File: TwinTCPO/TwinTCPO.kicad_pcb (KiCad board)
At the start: 2 copper layers, 83.8 x 45.1 mm, 44 parts, among them J1 Power, J2 Key, J3 Spk, J4 Phone, Q1 2N4401, Q2 2N7000, Q3 2N4401, Q4 2N4401, Q5 2N4403, U1 LM386

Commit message: Sync schematic and PCB
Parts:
- R6: value 10K -> 18K
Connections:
- J2 pad 3: Net-(J2-Pad3) -> unconnected-(J2-Pad3)
- J4 pad 10: Net-(J4-Pad10) -> unconnected-(J4-Pad10)
- RV3 pad 1: Net-(RV3-Pad1) -> unconnected-(RV3-Pad1)

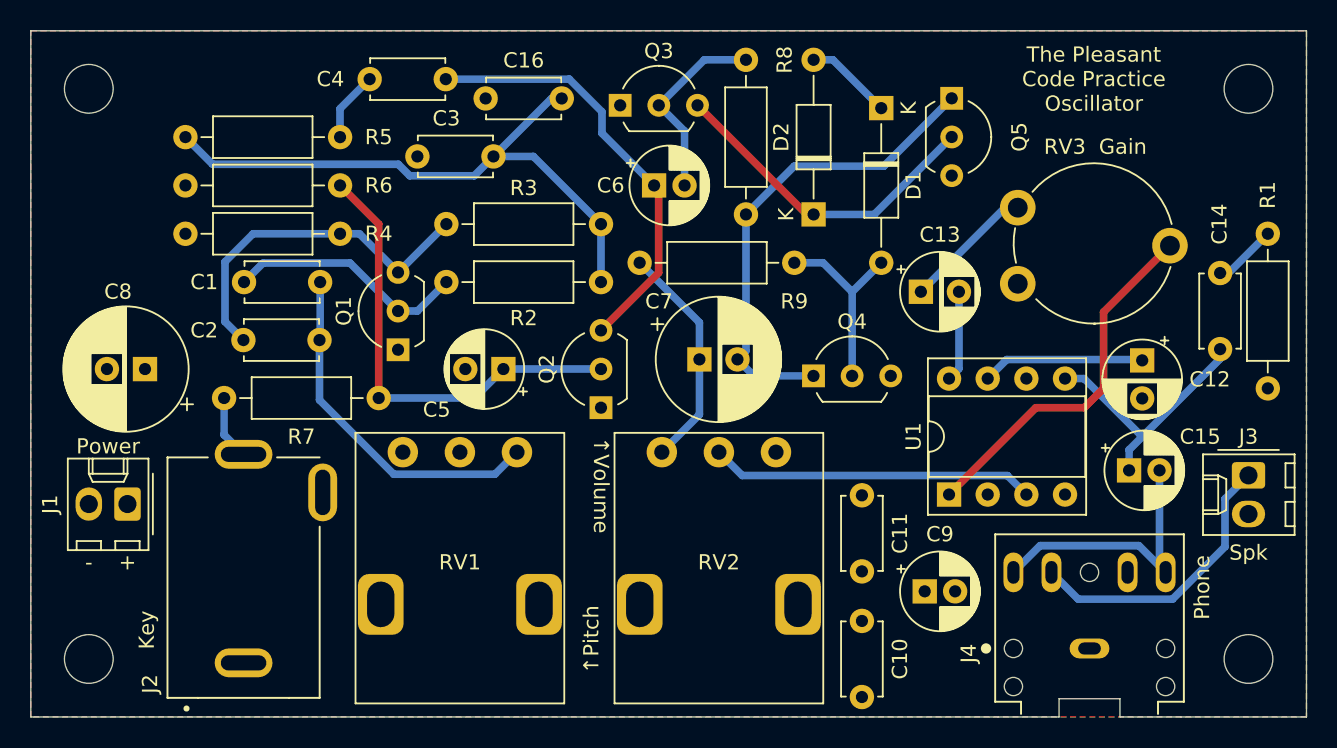
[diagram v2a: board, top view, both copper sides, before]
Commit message: Start at version 2
* Remove headphone jack
* Change R2/R3 for lower frequency
* Add 2.2K resistor in series with RV1
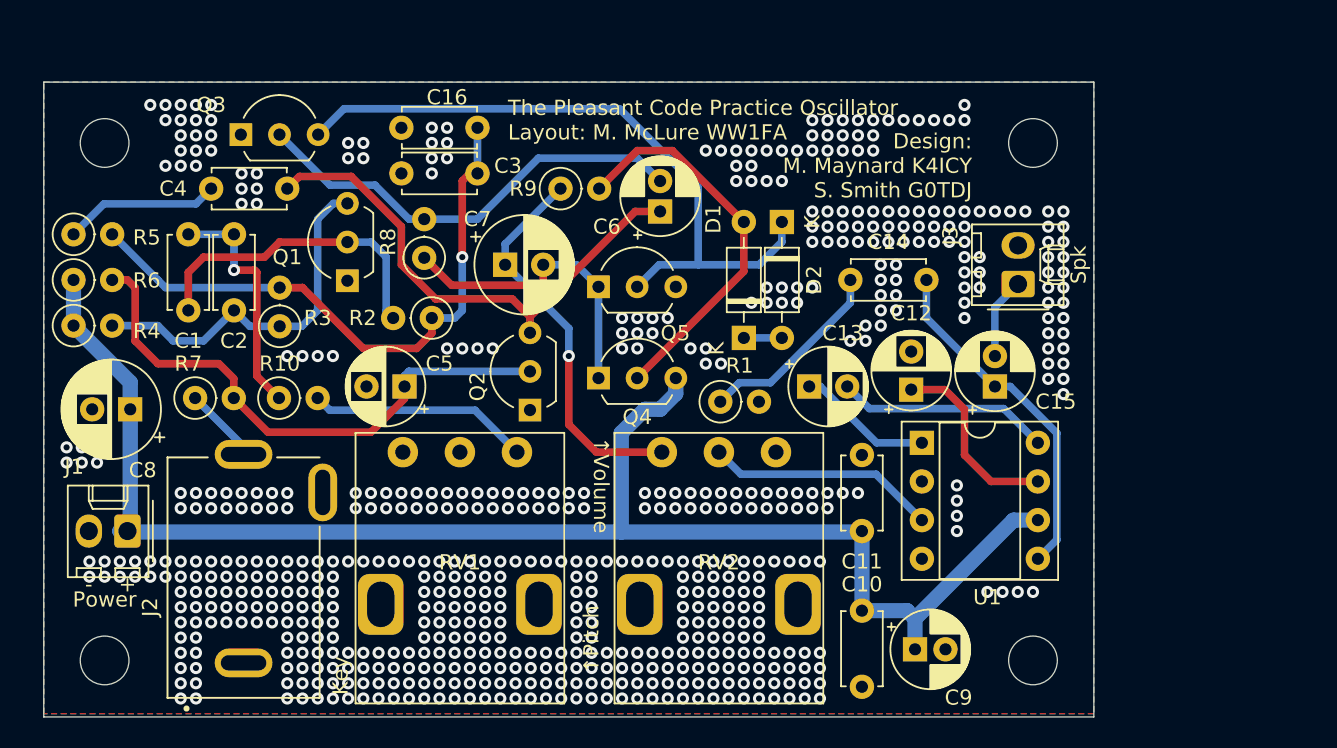
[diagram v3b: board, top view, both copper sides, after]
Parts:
- removed J4: Phone, MyLibrary:CUI_SJ1-3525N
- removed RV3: 10K, Potentiometer_THT:Potentiometer_Piher_PT-10-V10_Vertical
- added R10: 2.2K, Resistor_THT:R_Axial_DIN0207_L6.3mm_D2.5mm_P2.54mm_Vertical, F.Cu at (73.5, 111.8)
- C7, C8: footprint Capacitor_THT:CP_Radial_D8.0mm_P2.50mm -> Capacitor_THT:CP_Radial_D6.3mm_P2.50mm
- D1, D2: footprint Diode_THT:D_DO-35_SOD27_P10.16mm_Horizontal -> Diode_THT:D_DO-35_SOD27_P7.62mm_Horizontal
- R1, R4, R5, R6, R7, R8, R9: footprint Resistor_THT:R_Axial_DIN0207_L6.3mm_D2.5mm_P10.16mm_Horizontal -> Resistor_THT:R_Axial_DIN0207_L6.3mm_D2.5mm_P2.54mm_Vertical
- R2, R3: value 33K -> 47K; footprint Resistor_THT:R_Axial_DIN0207_L6.3mm_D2.5mm_P10.16mm_Horizontal -> Resistor_THT:R_Axial_DIN0207_L6.3mm_D2.5mm_P2.54mm_Vertical
- moved R1 37.6 mm to (102.5, 112.0), turned to 0 degrees
- moved Q5 26.3 mm to (94.5, 104.5), turned to 0 degrees
- moved Q3 25.0 mm to (71.0, 94.5)
- moved R8 21.3 mm to (83.0, 102.5)
- moved C14 19.8 mm to (116.0, 104.0), turned to 180 degrees
- moved J3 19.7 mm to (122.0, 104.3), turned to 90 degrees
- moved R5 18.6 mm to (60.0, 101.0), turned to 0 degrees
- moved D1 17.6 mm to (104.0, 107.8), turned to 90 degrees
- moved C12 15.3 mm to (115.0, 111.2), turned to 90 degrees
- moved H3 14.6 mm to (123.0, 95.0)
- moved C7 14.2 mm to (88.3, 103.0)
- moved H4 14.2 mm to (123.0, 129.0)
- moved Q4 14.1 mm to (94.5, 110.5)
- moved R3 12.8 mm to (73.5, 107.0), turned to 90 degrees
- moved C4 12.7 mm to (69.0, 98.0)
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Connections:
- J3 pad 1: Net-(J3-Pad1) -> Net-(C15-Pad2)
- RV1 pad 1: Net-(C1-Pad1) -> Net-(R10-Pad2)
- U1 pad 1: Net-(RV3-Pad2) -> Net-(C13-Pad1)
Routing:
- net VCC: track 0.00 -> 100.9 mm
- net Net-(RV3-Pad2): track 24.2 -> 0.00 mm
- net Net-(D2-Pad1): track 21.8 -> 44.9 mm
- net Net-(J3-Pad1): track 18.9 -> 0.00 mm
- net Net-(C6-Pad2): track 12.9 -> 29.6 mm
- net Net-(R10-Pad2): track 0.00 -> 14.6 mm
- net Net-(D1-Pad2): track 12.8 -> 25.6 mm
- net Net-(C15-Pad2): track 17.8 -> 5.36 mm
- net Net-(C7-Pad2): track 31.9 -> 20.0 mm
- net Net-(C7-Pad1): track 15.1 -> 25.6 mm, vias 0 -> 1
- net Net-(C14-Pad2): track 4.20 -> 12.7 mm
- net Net-(C13-Pad2): track 5.97 -> 14.1 mm
- net Net-(C1-Pad1): track 23.4 -> 15.8 mm, vias 0 -> 1
- net Net-(C5-Pad1): track 30.4 -> 36.9 mm
- net Net-(RV2-Pad2): track 21.4 -> 15.2 mm
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- added copper zone on B.Cu, net GND
- removed copper zone on B.Cu, net VCC
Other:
- board size 83.8 x 45.1 mm -> 69 x 41.7 mm
- board text added: "Design: M. Maynard K4ICY S. Smith G0TDJ"
- board text added: "The Pleasant Code Practice Oscillator Layout: M. McLure WW1FA"
- board text removed: "Gain"
- board text removed: "Layout by M. McLure WW1FA Based on work by M. Maynard K4ICY and S. Smith G0TDJ"
- board text removed: "Phone"
- board text removed: "The Pleasant Code Practice Oscillator"
